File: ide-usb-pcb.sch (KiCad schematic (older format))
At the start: 36 parts, among them J1 Conn_02x20_Odd_Even, J2 STM32F4_Discovery_Header, J3 Screw_Terminal_01x02, J4 USB_B, J5 Conn_01x01_Male, J6 Conn_01x03_Male, J7 Conn_01x02_Male, J8 Conn_01x01_Male, J9 Conn_01x01_Male, U1 TXS0108EPW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

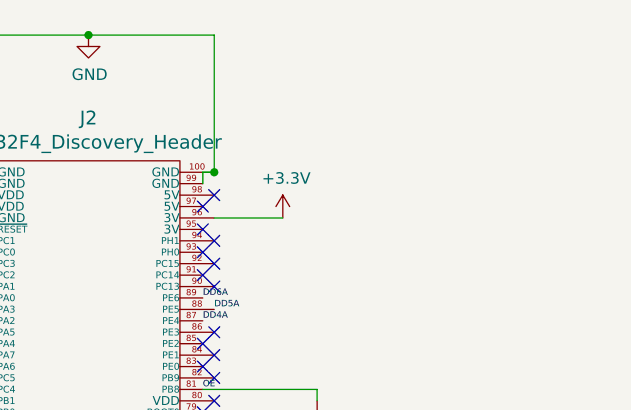
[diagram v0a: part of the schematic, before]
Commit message: Add jumper to power STM discovery board
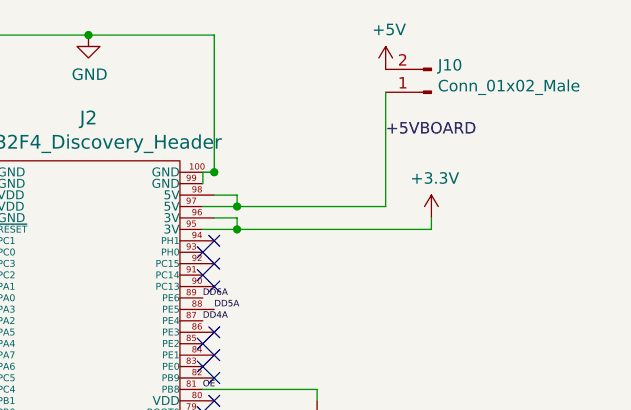
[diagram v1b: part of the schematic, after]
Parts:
- added J10: Conn_01x02_Male, Socket_Strips:Socket_Strip_Straight_1x02_Pitch2.54mm, symbol Connector:Conn_01x02_Male
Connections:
- net +3V3: now also J2.95 (3V)
- net +5V: now also J10.2 (Pin_2)
- net +5VBOARD: now reaches J2.97 (5V)
- net +5VBOARD: now also J2.98 (5V), J10.1 (Pin_1)
- no-connect marks 69 -> 66
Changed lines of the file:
@@
 L power:+3.3V #PWR010
 U 1 1 60E8794A
-P 9050 1650
-F 0 "#PWR010" H 9050 1500 50  0001 C CNN
-F 1 "+3.3V" H 9065 1823 50  0000 C CNN
-F 2 "" H 9050 1650 50  0001 C CNN
-F 3 "" H 9050 1650 50  0001 C CNN
-	1    9050 1650
-	1    0    0    -1
-$EndComp
-Wire Wire Line
-	9050 1650 8750 1650
+P 9700 1650
+F 0 "#PWR010" H 9700 1500 50  0001 C CNN
+F 1 "+3.3V" H 9715 1823 50  0000 C CNN
+F 2 "" H 9700 1650 50  0001 C CNN
+F 3 "" H 9700 1650 50  0001 C CNN
+	1    9700 1650
+	1    0    0    -1
+$EndComp
 $Comp
 L power:GND #PWR09
@@
 NoConn ~ 7650 1550
 NoConn ~ 7700 1600
-NoConn ~ 8700 1600
-NoConn ~ 8750 1550
 NoConn ~ 7650 1650
 NoConn ~ 7700 1700
@@
 NoConn ~ 8700 1800
 NoConn ~ 8750 1750
-NoConn ~ 8700 1700
 NoConn ~ 7700 2000
 Text Label 1250 1600 0    50   ~ 0
@@
 	1    0    0    -1
 $EndComp
+Wire Wire Line
+	8700 1700 8850 1700
+Wire Wire Line
+	9700 1700 9700 1650
+$Comp
+L Connector:Conn_01x02_Male J10
+U 1 1 60ED82F5
+P 9700 1100
+F 0 "J10" H 9672 982 50  0000 R CNN
+F 1 "Conn_01x02_Male" H 9672 1073 50  0000 R CNN
+F 2 "Socket_Strips:Socket_Strip_Straight_1x02_Pitch2.54mm" H 9700 1100 50  0001 C CNN
+F 3 "~" H 9700 1100 50  0001 C CNN
+	1    9700 1100
+	-1   0    0    1
+$EndComp
+Wire Wire Line
+	9500 1600 8850 1600
+Wire Wire Line
+	8750 1550 8850 1550
+Wire Wire Line
+	8850 1550 8850 1600
+Connection ~ 8850 1600
+Wire Wire Line
+	8850 1600 8700 1600
+Wire Wire Line
+	8750 1650 8850 1650
+Wire Wire Line
+	8850 1650 8850 1700
+Connection ~ 8850 1700
+Wire Wire Line
+	8850 1700 9700 1700
+$Comp
+L power:+5V #PWR016
+U 1 1 60EE1C61
+P 9500 1000
+F 0 "#PWR016" H 9500 850 50  0001 C CNN
+F 1 "+5V" H 9515 1173 50  0000 C CNN
+F 2 "" H 9500 1000 50  0001 C CNN
+F 3 "" H 9500 1000 50  0001 C CNN
+	1    9500 1000
+	1    0    0    -1
+$EndComp
+Wire Wire Line
+	9500 1100 9500 1600
+Text Label 9500 1300 0    50   ~ 0
++5VBOARD
 $EndSCHEMATC
